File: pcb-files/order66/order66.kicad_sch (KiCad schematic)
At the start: 144 parts, among them J1 NICEVIEW, J2 Pouch Battery Connector, SW1 AUX1, SW10 A, SW11 Z, SW12 AUX7, SW13 RST, SW14 2, SW15 W, SW16 S, SW17 X, SW18 LALT, SW19 ON/OFF, SW2 ESC, SW20 3, SW21 E, SW22 D, SW23 C, SW24 GUI, SW25 AUX5, SW26 4, SW27 R, SW28 F, SW29 V, SW3 TAB, SW30 RAISE, SW31 AUX4, SW32 5, SW33 T, SW34 G, SW35 B, SW36 AUX3, SW37 AUX2, SW38 6, SW39 Y, SW4 CAPSLCK, SW40 H, SW41 N, SW42 RSPACE, SW44 7, SW45 U, SW46 J, SW47 M, SW48 LOWER, SW5 LSHIFT, SW50 8, SW51 I, SW52 K, SW53 ,<, SW54 LEFT, SW56 9, SW57 O, SW58 L, SW59 .>, SW6 LCTRL, SW60 DOWN, SW62 0, SW63 P, SW64 ;:, SW65 /?, SW66 UP, SW67 AUX6, SW68 BACKSPACE, SW69 BACKSLACH, SW7 LSPACE, SW70 ENTER, SW71 RSHIFT, SW72 RIGHT, SW8 1, SW9 Q, U1 NiceNano

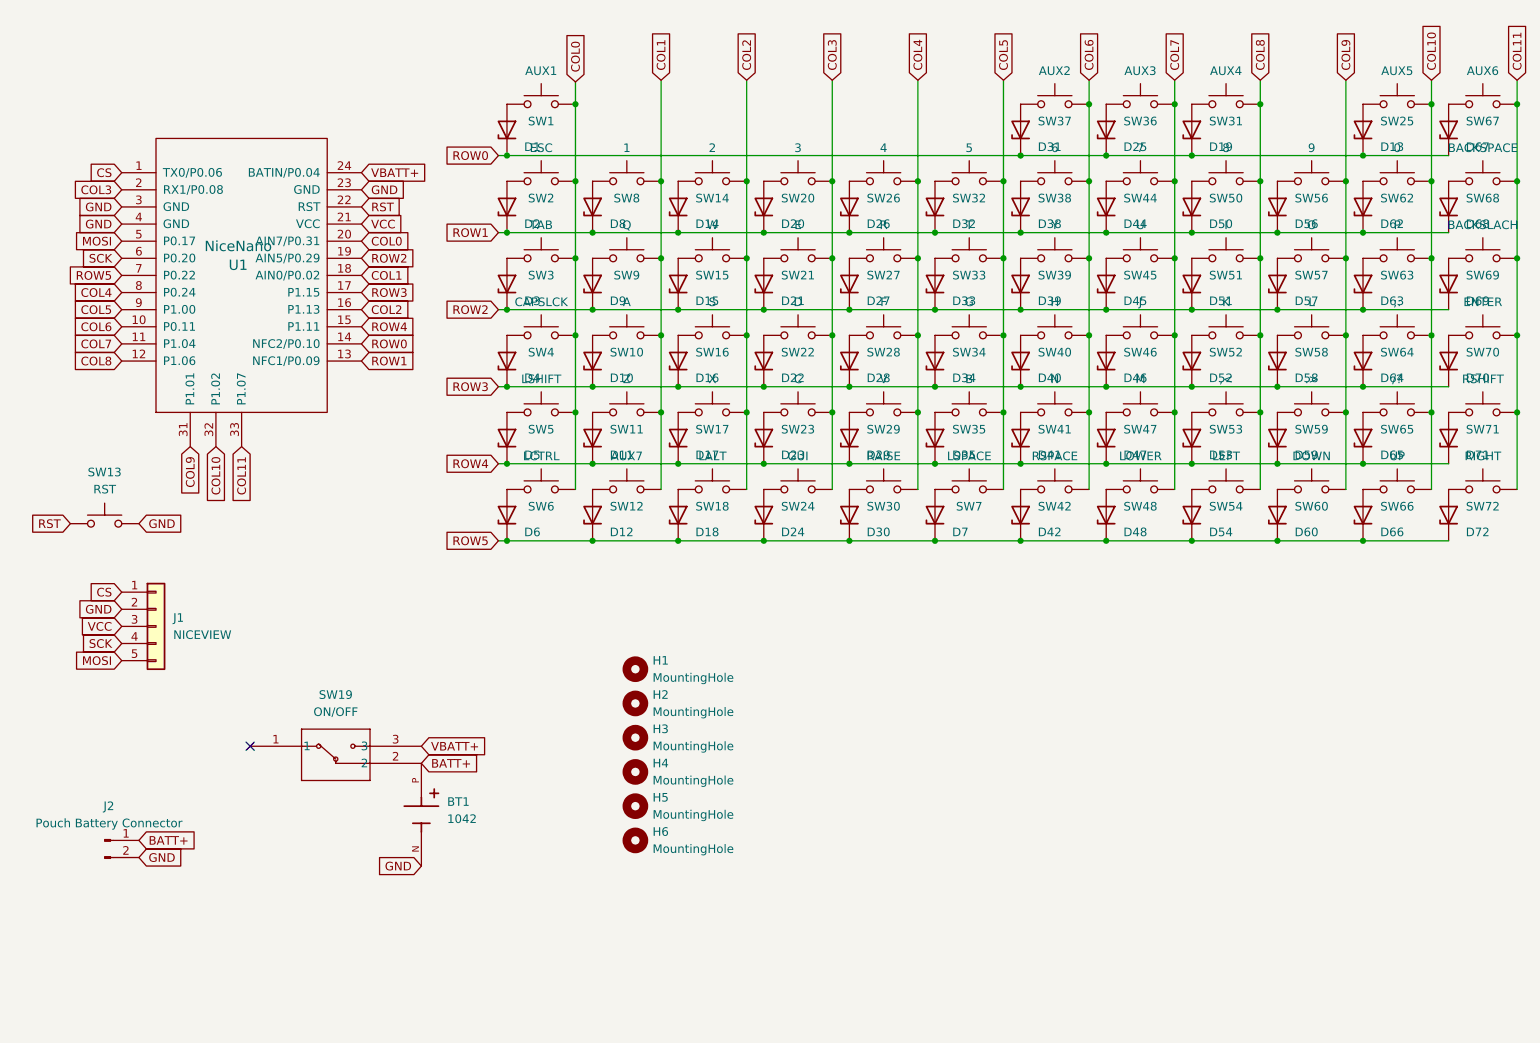
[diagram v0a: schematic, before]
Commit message: Trying though hole diodes (#1)
* changed to through hole diodes in schematic

* moved to more through hole components and rerouted traces

* trying to generate bom

* reordered the switch and diode numberings to be in order

* fixing and checking on board design rules to match pcb fabrication

* starting work on case

* reorganizing now that case files exists

* added support for millmax spring loaded swd pins for bootloader support
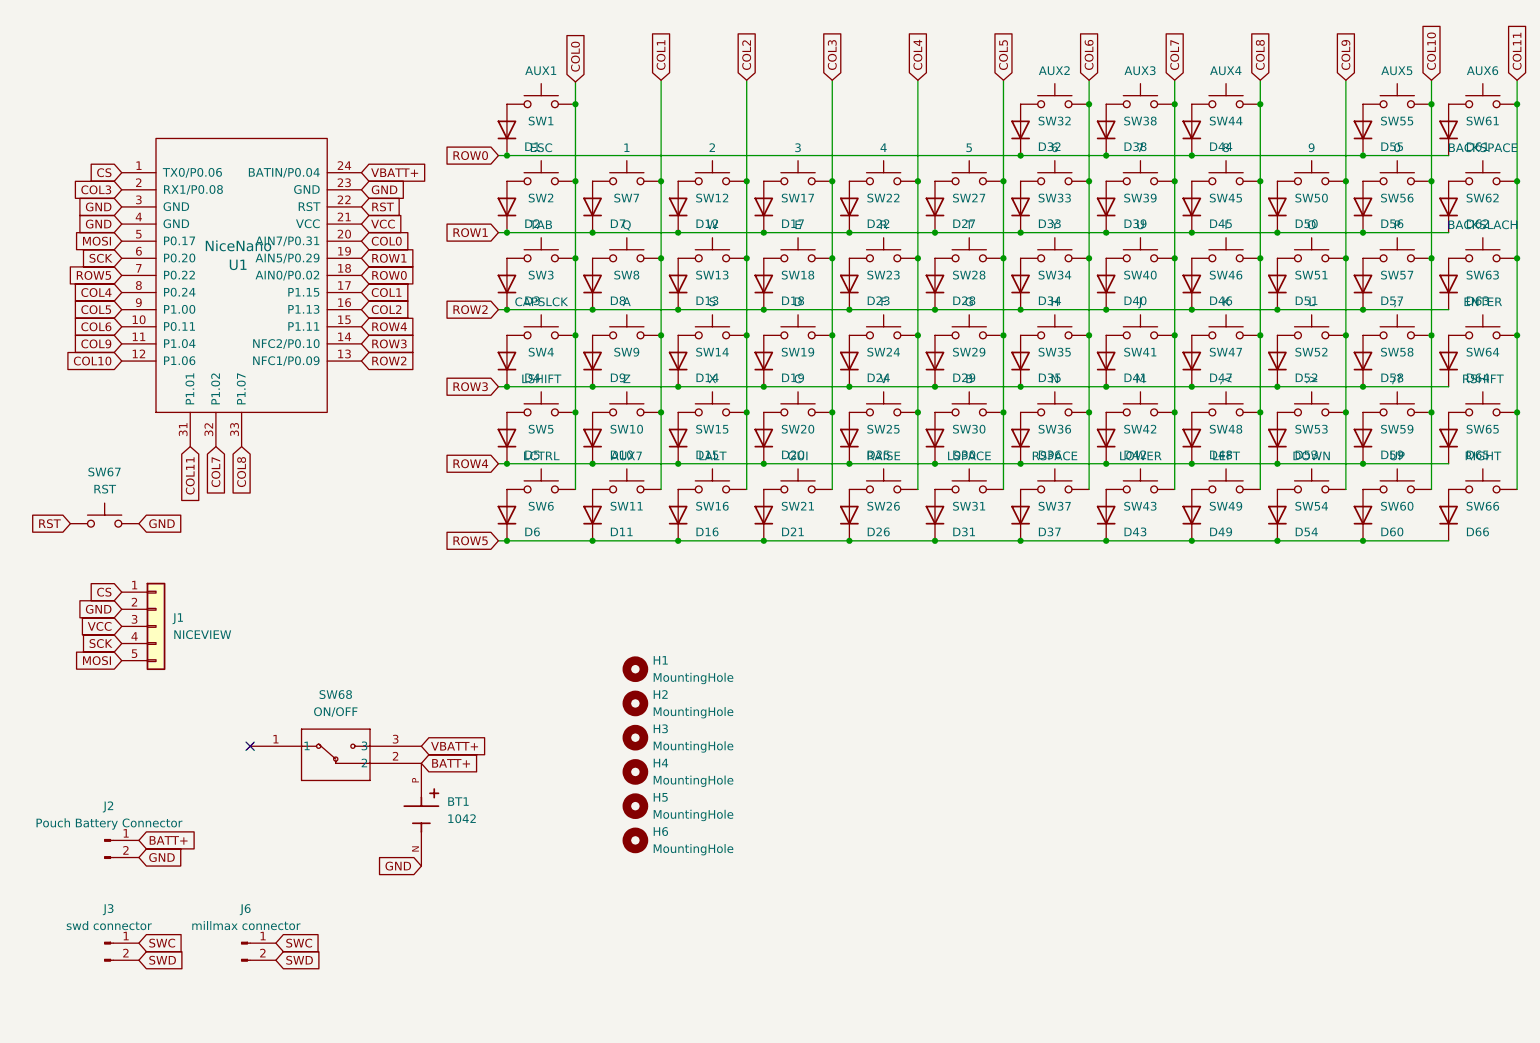
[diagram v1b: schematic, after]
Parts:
- added J3: swd connector, Connector_PinHeader_2.54mm:PinHeader_1x02_P2.54mm_Horizontal, symbol Connector:Conn_01x02_Pin
- added J6: millmax connector, Connector_PinHeader_2.54mm:PinHeader_1x02_P2.54mm_Vertical, symbol Connector:Conn_01x02_Pin
- BT1: footprint 1042:BAT_1042 -> 1043P:BAT_1043P; symbol 1042:1042 -> 1043:1043P; PARTREV E -> D; SNAPEDA_PN 1042 -> 1043P
- D1, D2, D3, D4, D5, D6: value 1N47xxA -> 1N4148; footprint Diode_SMD:D_SOD-123 -> Diode_THT:D_DO-35_SOD27_P7.62mm_Horizontal; symbol Diode:1N47xxA -> Diode:1N4148
- D10: renamed from D11; value 1N47xxA -> 1N4148; footprint Diode_SMD:D_SOD-123 -> Diode_THT:D_DO-35_SOD27_P7.62mm_Horizontal; symbol Diode:1N47xxA -> Diode:1N4148
- D11: renamed from D12; value 1N47xxA -> 1N4148; footprint Diode_SMD:D_SOD-123 -> Diode_THT:D_DO-35_SOD27_P7.62mm_Horizontal; symbol Diode:1N47xxA -> Diode:1N4148
- D12: renamed from D14; value 1N47xxA -> 1N4148; footprint Diode_SMD:D_SOD-123 -> Diode_THT:D_DO-35_SOD27_P7.62mm_Horizontal; symbol Diode:1N47xxA -> Diode:1N4148
- D13: renamed from D15; value 1N47xxA -> 1N4148; footprint Diode_SMD:D_SOD-123 -> Diode_THT:D_DO-35_SOD27_P7.62mm_Horizontal; symbol Diode:1N47xxA -> Diode:1N4148
- D14: renamed from D16; value 1N47xxA -> 1N4148; footprint Diode_SMD:D_SOD-123 -> Diode_THT:D_DO-35_SOD27_P7.62mm_Horizontal; symbol Diode:1N47xxA -> Diode:1N4148
- D15: renamed from D17; value 1N47xxA -> 1N4148; footprint Diode_SMD:D_SOD-123 -> Diode_THT:D_DO-35_SOD27_P7.62mm_Horizontal; symbol Diode:1N47xxA -> Diode:1N4148
- D16: renamed from D18; value 1N47xxA -> 1N4148; footprint Diode_SMD:D_SOD-123 -> Diode_THT:D_DO-35_SOD27_P7.62mm_Horizontal; symbol Diode:1N47xxA -> Diode:1N4148
- D17: renamed from D20; value 1N47xxA -> 1N4148; footprint Diode_SMD:D_SOD-123 -> Diode_THT:D_DO-35_SOD27_P7.62mm_Horizontal; symbol Diode:1N47xxA -> Diode:1N4148
- D18: renamed from D21; value 1N47xxA -> 1N4148; footprint Diode_SMD:D_SOD-123 -> Diode_THT:D_DO-35_SOD27_P7.62mm_Horizontal; symbol Diode:1N47xxA -> Diode:1N4148
- D19: renamed from D22; value 1N47xxA -> 1N4148; footprint Diode_SMD:D_SOD-123 -> Diode_THT:D_DO-35_SOD27_P7.62mm_Horizontal; symbol Diode:1N47xxA -> Diode:1N4148
- D20: renamed from D23; value 1N47xxA -> 1N4148; footprint Diode_SMD:D_SOD-123 -> Diode_THT:D_DO-35_SOD27_P7.62mm_Horizontal; symbol Diode:1N47xxA -> Diode:1N4148
- D21: renamed from D24; value 1N47xxA -> 1N4148; footprint Diode_SMD:D_SOD-123 -> Diode_THT:D_DO-35_SOD27_P7.62mm_Horizontal; symbol Diode:1N47xxA -> Diode:1N4148
- D22: renamed from D26; value 1N47xxA -> 1N4148; footprint Diode_SMD:D_SOD-123 -> Diode_THT:D_DO-35_SOD27_P7.62mm_Horizontal; symbol Diode:1N47xxA -> Diode:1N4148
- D23: renamed from D27; value 1N47xxA -> 1N4148; footprint Diode_SMD:D_SOD-123 -> Diode_THT:D_DO-35_SOD27_P7.62mm_Horizontal; symbol Diode:1N47xxA -> Diode:1N4148
- D24: renamed from D28; value 1N47xxA -> 1N4148; footprint Diode_SMD:D_SOD-123 -> Diode_THT:D_DO-35_SOD27_P7.62mm_Horizontal; symbol Diode:1N47xxA -> Diode:1N4148
- D25: renamed from D29; value 1N47xxA -> 1N4148; footprint Diode_SMD:D_SOD-123 -> Diode_THT:D_DO-35_SOD27_P7.62mm_Horizontal; symbol Diode:1N47xxA -> Diode:1N4148
- D26: renamed from D30; value 1N47xxA -> 1N4148; footprint Diode_SMD:D_SOD-123 -> Diode_THT:D_DO-35_SOD27_P7.62mm_Horizontal; symbol Diode:1N47xxA -> Diode:1N4148
- D27: renamed from D32; value 1N47xxA -> 1N4148; footprint Diode_SMD:D_SOD-123 -> Diode_THT:D_DO-35_SOD27_P7.62mm_Horizontal; symbol Diode:1N47xxA -> Diode:1N4148
- D28: renamed from D33; value 1N47xxA -> 1N4148; footprint Diode_SMD:D_SOD-123 -> Diode_THT:D_DO-35_SOD27_P7.62mm_Horizontal; symbol Diode:1N47xxA -> Diode:1N4148
- D29: renamed from D34; value 1N47xxA -> 1N4148; footprint Diode_SMD:D_SOD-123 -> Diode_THT:D_DO-35_SOD27_P7.62mm_Horizontal; symbol Diode:1N47xxA -> Diode:1N4148
- D30: renamed from D35; value 1N47xxA -> 1N4148; footprint Diode_SMD:D_SOD-123 -> Diode_THT:D_DO-35_SOD27_P7.62mm_Horizontal; symbol Diode:1N47xxA -> Diode:1N4148
- D31: renamed from D7; value 1N47xxA -> 1N4148; footprint Diode_SMD:D_SOD-123 -> Diode_THT:D_DO-35_SOD27_P7.62mm_Horizontal; symbol Diode:1N47xxA -> Diode:1N4148
- D32: renamed from D31; value 1N47xxA -> 1N4148; footprint Diode_SMD:D_SOD-123 -> Diode_THT:D_DO-35_SOD27_P7.62mm_Horizontal; symbol Diode:1N47xxA -> Diode:1N4148
- D33: renamed from D38; value 1N47xxA -> 1N4148; footprint Diode_SMD:D_SOD-123 -> Diode_THT:D_DO-35_SOD27_P7.62mm_Horizontal; symbol Diode:1N47xxA -> Diode:1N4148
- D34: renamed from D39; value 1N47xxA -> 1N4148; footprint Diode_SMD:D_SOD-123 -> Diode_THT:D_DO-35_SOD27_P7.62mm_Horizontal; symbol Diode:1N47xxA -> Diode:1N4148
- D35: renamed from D40; value 1N47xxA -> 1N4148; footprint Diode_SMD:D_SOD-123 -> Diode_THT:D_DO-35_SOD27_P7.62mm_Horizontal; symbol Diode:1N47xxA -> Diode:1N4148
- D36: renamed from D41; value 1N47xxA -> 1N4148; footprint Diode_SMD:D_SOD-123 -> Diode_THT:D_DO-35_SOD27_P7.62mm_Horizontal; symbol Diode:1N47xxA -> Diode:1N4148
- D37: renamed from D42; value 1N47xxA -> 1N4148; footprint Diode_SMD:D_SOD-123 -> Diode_THT:D_DO-35_SOD27_P7.62mm_Horizontal; symbol Diode:1N47xxA -> Diode:1N4148
- D38: renamed from D25; value 1N47xxA -> 1N4148; footprint Diode_SMD:D_SOD-123 -> Diode_THT:D_DO-35_SOD27_P7.62mm_Horizontal; symbol Diode:1N47xxA -> Diode:1N4148
- D39: renamed from D44; value 1N47xxA -> 1N4148; footprint Diode_SMD:D_SOD-123 -> Diode_THT:D_DO-35_SOD27_P7.62mm_Horizontal; symbol Diode:1N47xxA -> Diode:1N4148
- D40: renamed from D45; value 1N47xxA -> 1N4148; footprint Diode_SMD:D_SOD-123 -> Diode_THT:D_DO-35_SOD27_P7.62mm_Horizontal; symbol Diode:1N47xxA -> Diode:1N4148
- D41: renamed from D46; value 1N47xxA -> 1N4148; footprint Diode_SMD:D_SOD-123 -> Diode_THT:D_DO-35_SOD27_P7.62mm_Horizontal; symbol Diode:1N47xxA -> Diode:1N4148
- D42: renamed from D47; value 1N47xxA -> 1N4148; footprint Diode_SMD:D_SOD-123 -> Diode_THT:D_DO-35_SOD27_P7.62mm_Horizontal; symbol Diode:1N47xxA -> Diode:1N4148
- D43: renamed from D48; value 1N47xxA -> 1N4148; footprint Diode_SMD:D_SOD-123 -> Diode_THT:D_DO-35_SOD27_P7.62mm_Horizontal; symbol Diode:1N47xxA -> Diode:1N4148
- D44: renamed from D19; value 1N47xxA -> 1N4148; footprint Diode_SMD:D_SOD-123 -> Diode_THT:D_DO-35_SOD27_P7.62mm_Horizontal; symbol Diode:1N47xxA -> Diode:1N4148
- D45: renamed from D50; value 1N47xxA -> 1N4148; footprint Diode_SMD:D_SOD-123 -> Diode_THT:D_DO-35_SOD27_P7.62mm_Horizontal; symbol Diode:1N47xxA -> Diode:1N4148
- D46: renamed from D51; value 1N47xxA -> 1N4148; footprint Diode_SMD:D_SOD-123 -> Diode_THT:D_DO-35_SOD27_P7.62mm_Horizontal; symbol Diode:1N47xxA -> Diode:1N4148
- D47: renamed from D52; value 1N47xxA -> 1N4148; footprint Diode_SMD:D_SOD-123 -> Diode_THT:D_DO-35_SOD27_P7.62mm_Horizontal; symbol Diode:1N47xxA -> Diode:1N4148
- D48: renamed from D53; value 1N47xxA -> 1N4148; footprint Diode_SMD:D_SOD-123 -> Diode_THT:D_DO-35_SOD27_P7.62mm_Horizontal; symbol Diode:1N47xxA -> Diode:1N4148
- D49: renamed from D54; value 1N47xxA -> 1N4148; footprint Diode_SMD:D_SOD-123 -> Diode_THT:D_DO-35_SOD27_P7.62mm_Horizontal; symbol Diode:1N47xxA -> Diode:1N4148
- D50: renamed from D56; value 1N47xxA -> 1N4148; footprint Diode_SMD:D_SOD-123 -> Diode_THT:D_DO-35_SOD27_P7.62mm_Horizontal; symbol Diode:1N47xxA -> Diode:1N4148
- D51: renamed from D57; value 1N47xxA -> 1N4148; footprint Diode_SMD:D_SOD-123 -> Diode_THT:D_DO-35_SOD27_P7.62mm_Horizontal; symbol Diode:1N47xxA -> Diode:1N4148
- D52: renamed from D58; value 1N47xxA -> 1N4148; footprint Diode_SMD:D_SOD-123 -> Diode_THT:D_DO-35_SOD27_P7.62mm_Horizontal; symbol Diode:1N47xxA -> Diode:1N4148
- D53: renamed from D59; value 1N47xxA -> 1N4148; footprint Diode_SMD:D_SOD-123 -> Diode_THT:D_DO-35_SOD27_P7.62mm_Horizontal; symbol Diode:1N47xxA -> Diode:1N4148
- D54: renamed from D60; value 1N47xxA -> 1N4148; footprint Diode_SMD:D_SOD-123 -> Diode_THT:D_DO-35_SOD27_P7.62mm_Horizontal; symbol Diode:1N47xxA -> Diode:1N4148
- D55: renamed from D13; value 1N47xxA -> 1N4148; footprint Diode_SMD:D_SOD-123 -> Diode_THT:D_DO-35_SOD27_P7.62mm_Horizontal; symbol Diode:1N47xxA -> Diode:1N4148
- D56: renamed from D62; value 1N47xxA -> 1N4148; footprint Diode_SMD:D_SOD-123 -> Diode_THT:D_DO-35_SOD27_P7.62mm_Horizontal; symbol Diode:1N47xxA -> Diode:1N4148
- D57: renamed from D63; value 1N47xxA -> 1N4148; footprint Diode_SMD:D_SOD-123 -> Diode_THT:D_DO-35_SOD27_P7.62mm_Horizontal; symbol Diode:1N47xxA -> Diode:1N4148
- D58: renamed from D64; value 1N47xxA -> 1N4148; footprint Diode_SMD:D_SOD-123 -> Diode_THT:D_DO-35_SOD27_P7.62mm_Horizontal; symbol Diode:1N47xxA -> Diode:1N4148
- D59: renamed from D65; value 1N47xxA -> 1N4148; footprint Diode_SMD:D_SOD-123 -> Diode_THT:D_DO-35_SOD27_P7.62mm_Horizontal; symbol Diode:1N47xxA -> Diode:1N4148
- D60: renamed from D66; value 1N47xxA -> 1N4148; footprint Diode_SMD:D_SOD-123 -> Diode_THT:D_DO-35_SOD27_P7.62mm_Horizontal; symbol Diode:1N47xxA -> Diode:1N4148
- D61: renamed from D67; value 1N47xxA -> 1N4148; footprint Diode_SMD:D_SOD-123 -> Diode_THT:D_DO-35_SOD27_P7.62mm_Horizontal; symbol Diode:1N47xxA -> Diode:1N4148
- D62: renamed from D68; value 1N47xxA -> 1N4148; footprint Diode_SMD:D_SOD-123 -> Diode_THT:D_DO-35_SOD27_P7.62mm_Horizontal; symbol Diode:1N47xxA -> Diode:1N4148
- D63: renamed from D69; value 1N47xxA -> 1N4148; footprint Diode_SMD:D_SOD-123 -> Diode_THT:D_DO-35_SOD27_P7.62mm_Horizontal; symbol Diode:1N47xxA -> Diode:1N4148
- D64: renamed from D70; value 1N47xxA -> 1N4148; footprint Diode_SMD:D_SOD-123 -> Diode_THT:D_DO-35_SOD27_P7.62mm_Horizontal; symbol Diode:1N47xxA -> Diode:1N4148
- D65: renamed from D71; value 1N47xxA -> 1N4148; footprint Diode_SMD:D_SOD-123 -> Diode_THT:D_DO-35_SOD27_P7.62mm_Horizontal; symbol Diode:1N47xxA -> Diode:1N4148
- D66: renamed from D72; value 1N47xxA -> 1N4148; footprint Diode_SMD:D_SOD-123 -> Diode_THT:D_DO-35_SOD27_P7.62mm_Horizontal; symbol Diode:1N47xxA -> Diode:1N4148
- D7: renamed from D8; value 1N47xxA -> 1N4148; footprint Diode_SMD:D_SOD-123 -> Diode_THT:D_DO-35_SOD27_P7.62mm_Horizontal; symbol Diode:1N47xxA -> Diode:1N4148
- D8: renamed from D9; value 1N47xxA -> 1N4148; footprint Diode_SMD:D_SOD-123 -> Diode_THT:D_DO-35_SOD27_P7.62mm_Horizontal; symbol Diode:1N47xxA -> Diode:1N4148
- D9: renamed from D10; value 1N47xxA -> 1N4148; footprint Diode_SMD:D_SOD-123 -> Diode_THT:D_DO-35_SOD27_P7.62mm_Horizontal; symbol Diode:1N47xxA -> Diode:1N4148
- J2: footprint Connector_JST:JST_EH_S2B-EH_1x02_P2.50mm_Horizontal -> Connector_JST:JST_PH_B2B-PH-K_1x02_P2.00mm_Vertical
- SW67: renamed from SW13; footprint Button_Switch_SMD:SW_SPST_TL3342 -> Button_Switch_THT:SW_TH_Tactile_Omron_B3F-10xx
- renumbered SW11 to SW10, SW12 to SW11, SW14 to SW12, SW15 to SW13, SW16 to SW14, SW17 to SW15, SW18 to SW16, SW20 to SW17, SW21 to SW18, SW22 to SW19, SW23 to SW20, SW24 to SW21, SW26 to SW22, SW27 to SW23, SW28 to SW24, SW29 to SW25, SW30 to SW26, SW32 to SW27, SW33 to SW28, SW34 to SW29, SW35 to SW30, SW7 to SW31, SW37 to SW32, SW38 to SW33, SW39 to SW34, SW40 to SW35, SW41 to SW36, SW42 to SW37, SW36 to SW38, SW44 to SW39, SW45 to SW40, SW46 to SW41, SW47 to SW42, SW48 to SW43, SW31 to SW44, SW50 to SW45, SW51 to SW46, SW52 to SW47, SW53 to SW48, SW54 to SW49, SW56 to SW50, SW57 to SW51, SW58 to SW52, SW59 to SW53, SW60 to SW54, SW25 to SW55, SW62 to SW56, SW63 to SW57, SW64 to SW58, SW65 to SW59, SW66 to SW60, SW67 to SW61, SW68 to SW62, SW69 to SW63, SW70 to SW64, SW71 to SW65, SW72 to SW66, SW19 to SW68, SW8 to SW7, SW9 to SW8, SW10 to SW9
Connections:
- net COL1: now also U1.17 (P1.15); no longer U1.18 (AIN0/P0.02)
- net COL10: now also U1.12 (P1.06); no longer U1.32 (P1.02)
- net COL11: now also U1.31 (P1.01); no longer U1.33 (P1.07)
- net COL7: now also U1.32 (P1.02); no longer U1.11 (P1.04)
- net COL8: now also U1.33 (P1.07); no longer U1.12 (P1.06)
- net COL9: now also U1.11 (P1.04); no longer U1.31 (P1.01)
- net ROW0: now also U1.18 (AIN0/P0.02); no longer U1.14 (NFC2/P0.10)
- net ROW1: now also U1.19 (AIN5/P0.29); no longer U1.13 (NFC1/P0.09)
- net ROW2: now also U1.13 (NFC1/P0.09); no longer U1.19 (AIN5/P0.29)
- net ROW3: now also U1.14 (NFC2/P0.10); no longer U1.17 (P1.15)
- new net SWC: J3.1 (Pin_1), J6.1 (Pin_1)
- new net SWD: J3.2 (Pin_2), J6.2 (Pin_2)

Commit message: added the smd sod 123 package diode symbols. havent placed/routed all the footprints yet but seems to be okay. need to figure out what I want to do with the silkscreen references. probably should just place the base numbered one and dont use the other
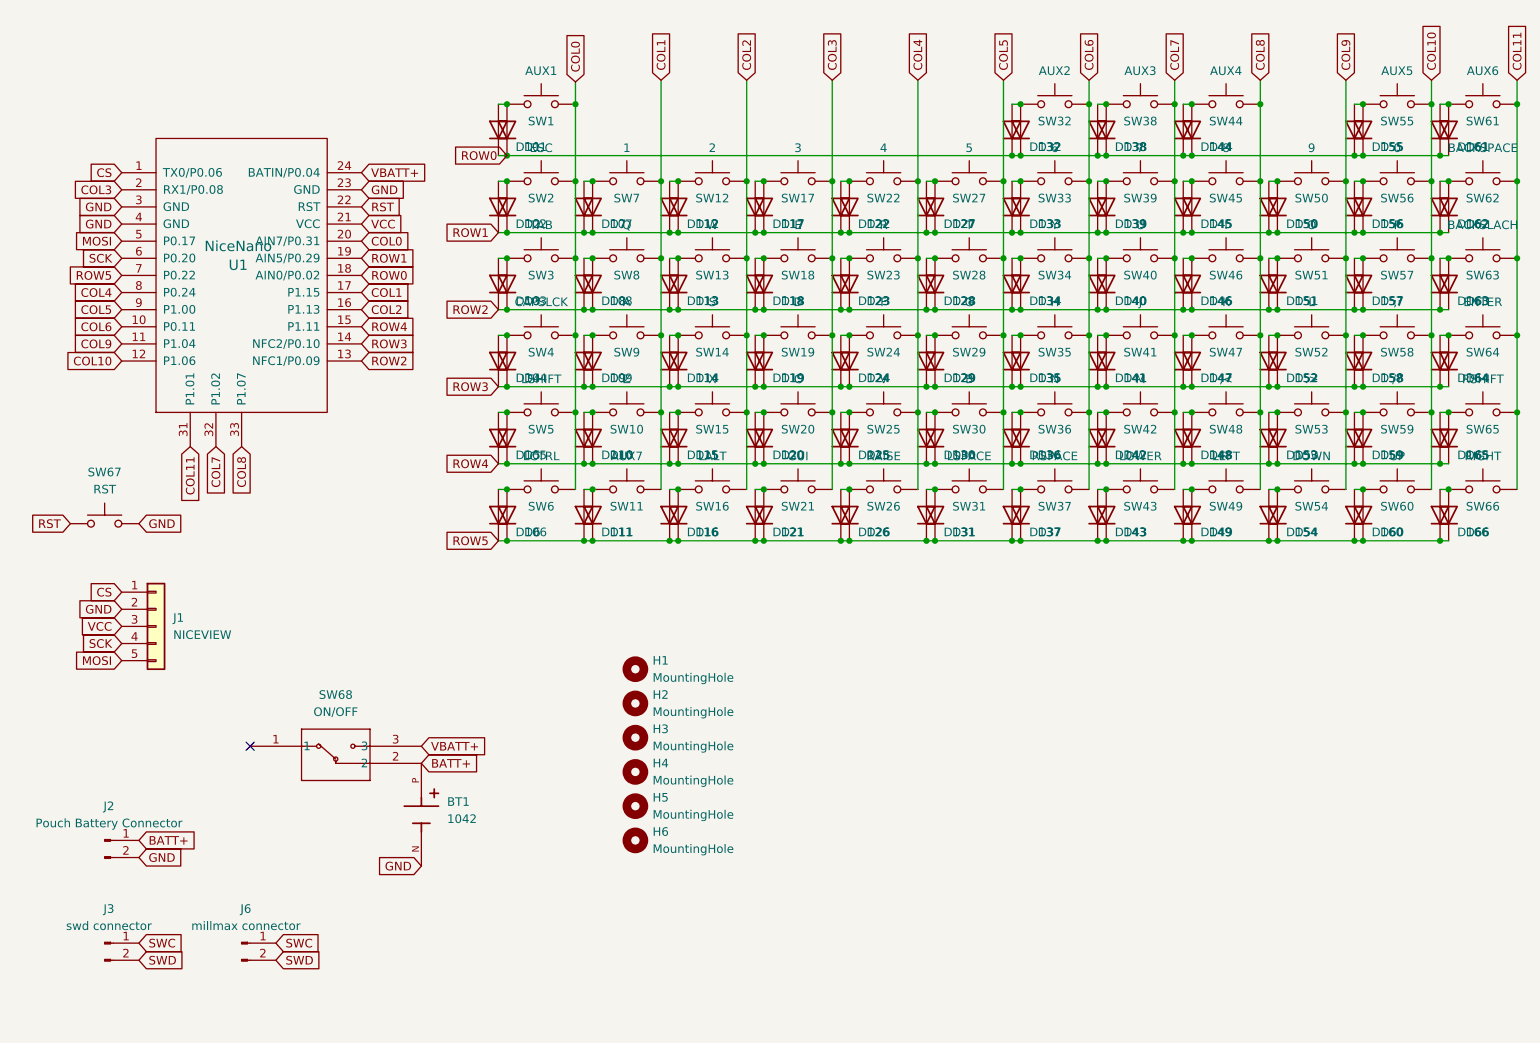
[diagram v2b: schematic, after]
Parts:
- added D101, D102, D103, D104, D105, D106, D107, D108, D109, D110, D111, D112, D113, D114, D115, D116, D117, D118, D119, D120, D121, D122, D123, D124, D125, D126, D127, D128, D129, D130, D131, D132, D133, D134, D135, D136, D137, D138, D139, D140, D141, D142, D143, D144, D145, D146, D147, D148, D149, D150, D151, D152, D153, D154, D155, D156, D157, D158, D159, D160, D161, D162, D163, D164, D165, D166: 1N4148, Diode_SMD:D_SOD-123, symbol Diode:1N4148W
- J6: note (none) -> try to find part number 8212200210001101 millmax spring loa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
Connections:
- net ROW0: now also D101.1 (K), D132.1 (K), D138.1 (K), D144.1 (K), D155.1 (K), D161.1 (K)
- net ROW1: now also D102.1 (K), D107.1 (K), D112.1 (K), D117.1 (K), D122.1 (K), D127.1 (K), D133.1 (K), D139.1 (K), D145.1 (K), D150.1 (K), D156.1 (K), D162.1 (K)
- net ROW2: now also D103.1 (K), D108.1 (K), D113.1 (K), D118.1 (K), D123.1 (K), D128.1 (K), D134.1 (K), D140.1 (K), D146.1 (K), D151.1 (K), D157.1 (K), D163.1 (K)
- net ROW3: now also D104.1 (K), D109.1 (K), D114.1 (K), D119.1 (K), D124.1 (K), D129.1 (K), D135.1 (K), D141.1 (K), D147.1 (K), D152.1 (K), D158.1 (K), D164.1 (K)
- net ROW4: now also D105.1 (K), D110.1 (K), D115.1 (K), D120.1 (K), D125.1 (K), D130.1 (K), D136.1 (K), D142.1 (K), D148.1 (K), D153.1 (K), D159.1 (K), D165.1 (K)
- net ROW5: now also D106.1 (K), D111.1 (K), D116.1 (K), D121.1 (K), D126.1 (K), D131.1 (K), D137.1 (K), D143.1 (K), D149.1 (K), D154.1 (K), D160.1 (K), D166.1 (K)
- net at D51.2 (A), SW51.1: now also D151.2 (A)
- net at D54.2 (A), SW54.1: now also D154.2 (A)
- net at D16.2 (A), SW16.1: now also D116.2 (A)
- net at D42.2 (A), SW42.1: now also D142.2 (A)
- net at D24.2 (A), SW24.1: now also D124.2 (A)
- net at D19.2 (A), SW19.1: now also D119.2 (A)
- net at D8.2 (A), SW8.1: now also D108.2 (A)
- net at D10.2 (A), SW10.1: now also D110.2 (A)
- net at D66.2 (A), SW66.1: now also D166.2 (A)
- net at D23.2 (A), SW23.1: now also D123.2 (A)
- net at D50.2 (A), SW50.1: now also D150.2 (A)
- net at D5.2 (A), SW5.1: now also D105.2 (A)
- net at D39.2 (A), SW39.1: now also D139.2 (A)
- net at D38.2 (A), SW38.1: now also D138.2 (A)
- net at D2.2 (A), SW2.1: now also D102.2 (A)
- net at D48.2 (A), SW48.1: now also D148.2 (A)
- net at D33.2 (A), SW33.1: now also D133.2 (A)
- net at D57.2 (A), SW57.1: now also D157.2 (A)
- net at D59.2 (A), SW59.1: now also D159.2 (A)
- net at D9.2 (A), SW9.1: now also D109.2 (A)
- net at D62.2 (A), SW62.1: now also D162.2 (A)
- net at D17.2 (A), SW17.1: now also D117.2 (A)
- net at D56.2 (A), SW56.1: now also D156.2 (A)
- net at D64.2 (A), SW64.1: now also D164.2 (A)
- net at D6.2 (A), SW6.1: now also D106.2 (A)
- net at D58.2 (A), SW58.1: now also D158.2 (A)
- net at D36.2 (A), SW36.1: now also D136.2 (A)
- net at D61.2 (A), SW61.1: now also D161.2 (A)
- net at D11.2 (A), SW11.1: now also D111.2 (A)
- net at D41.2 (A), SW41.1: now also D141.2 (A)
- net at D44.2 (A), SW44.1: now also D144.2 (A)
- net at D46.2 (A), SW46.1: now also D146.2 (A)
- net at D60.2 (A), SW60.1: now also D160.2 (A)
- net at D15.2 (A), SW15.1: now also D115.2 (A)
- net at D4.2 (A), SW4.1: now also D104.2 (A)
- net at D55.2 (A), SW55.1: now also D155.2 (A)
- net at D13.2 (A), SW13.1: now also D113.2 (A)
- net at D37.2 (A), SW37.1: now also D137.2 (A)
- net at D12.2 (A), SW12.1: now also D112.2 (A)
- net at D65.2 (A), SW65.1: now also D165.2 (A)
- net at D18.2 (A), SW18.1: now also D118.2 (A)
- net at D47.2 (A), SW47.1: now also D147.2 (A)
- net at D43.2 (A), SW43.1: now also D143.2 (A)
- net at D35.2 (A), SW35.1: now also D135.2 (A)
- net at D52.2 (A), SW52.1: now also D152.2 (A)
- net at D26.2 (A), SW26.1: now also D126.2 (A)
- net at D29.2 (A), SW29.1: now also D129.2 (A)
- net at D34.2 (A), SW34.1: now also D134.2 (A)
- net at D49.2 (A), SW49.1: now also D149.2 (A)
- net at D31.2 (A), SW31.1: now also D131.2 (A)
- net at D45.2 (A), SW45.1: now also D145.2 (A)
- net at D27.2 (A), SW27.1: now also D127.2 (A)
- net at D7.2 (A), SW7.1: now also D107.2 (A)
- net at D53.2 (A), SW53.1: now also D153.2 (A)
- net at D21.2 (A), SW21.1: now also D121.2 (A)
- net at D20.2 (A), SW20.1: now also D120.2 (A)
- net at D28.2 (A), SW28.1: now also D128.2 (A)
- net at D1.2 (A), SW1.1: now also D101.2 (A)
- net at D3.2 (A), SW3.1: now also D103.2 (A)
- net at D40.2 (A), SW40.1: now also D140.2 (A)
- net at D25.2 (A), SW25.1: now also D125.2 (A)
- net at D63.2 (A), SW63.1: now also D163.2 (A)
- net at D30.2 (A), SW30.1: now also D130.2 (A)
- net at D14.2 (A), SW14.1: now also D114.2 (A)
- net at D32.2 (A), SW32.1: now also D132.2 (A)
- net at D22.2 (A), SW22.1: now also D122.2 (A)
